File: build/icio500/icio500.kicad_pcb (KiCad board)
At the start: 4 copper layers, 113 x 105 mm, 54 parts, among them J1 ?, U1 ?, U2 ?, U3 ?, U4 ?, U5 ?, U6 ?

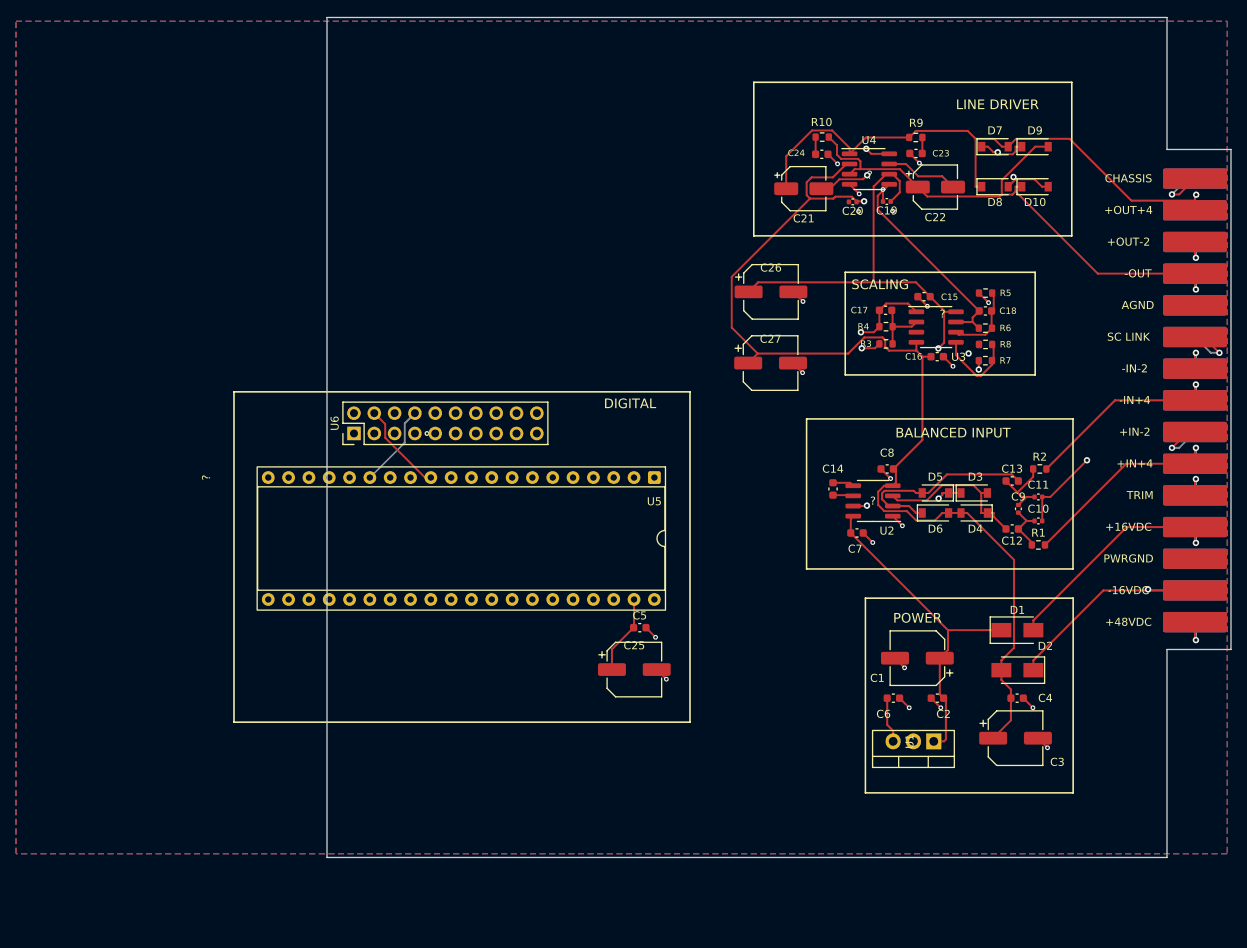
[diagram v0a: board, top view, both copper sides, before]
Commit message: Finalize VPR-500 dimensions and faceplate silkscreen
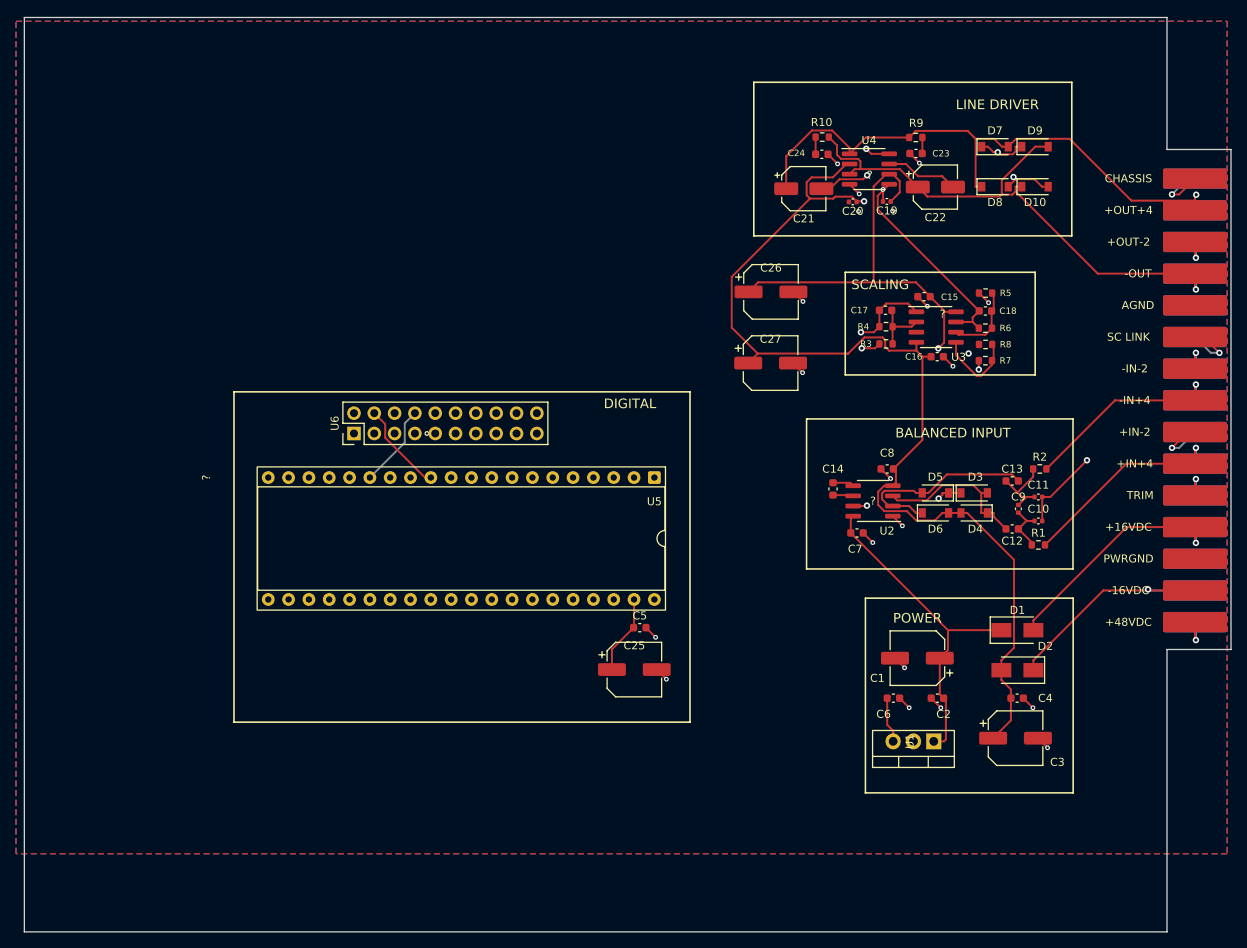
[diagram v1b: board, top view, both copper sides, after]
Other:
- board size 113 x 105 mm -> 150.8 x 114.3 mm
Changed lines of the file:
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@@
 	)
 	(gr_line
-		(start 90 160)
-		(end 90 55)
+		(start 52.17 55)
+		(end 195 55)
 		(stroke
 			(width 0.1)
@@
 	(gr_line
 		(start 195 55)
-		(end 90 55)
-		(stroke
-			(width 0.1)
-			(type default)
-		)
-		(layer "Edge.Cuts")
-	)
-	(gr_line
-		(start 195 71.5)
-		(end 195 55)
+		(end 195 71.5)
 		(stroke
 			(width 0.1)
@@
 		(start 195 71.5)
 		(end 203 71.5)
-		(stroke
-			(width 0.1)
-			(type default)
-		)
-		(layer "Edge.Cuts")
-	)
-	(gr_line
-		(start 195 134)
-		(end 195 160)
-		(stroke
-			(width 0.1)
-			(type default)
-		)
-		(layer "Edge.Cuts")
-	)
-	(gr_line
-		(start 195 160)
-		(end 90 160)
 		(stroke
 			(width 0.1)
@@
 		(stroke
 			(width 0.1)
+			(type default)
+		)
+		(layer "Edge.Cuts")
+	)
+	(gr_line
+		(start 195 134)
+		(end 195 169.3)
+		(stroke
+			(width 0.1)
+			(type default)
+		)
+		(layer "Edge.Cuts")
+	)
+	(gr_line
+		(start 195 169.3)
+		(end 52.17 169.3)
+		(stroke
+			(width 0.1)
+			(type default)
+		)
+		(layer "Edge.Cuts")
+	)
+	(gr_line
+		(start 52.17 169.3)
+		(end 52.17 55)
+		(stroke
+			(width 0.1)

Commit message: Autoroute remaining disconnected pads (GND, faceplate, Daisy)
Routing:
- net gnd: track 32.0 -> 221.5 mm
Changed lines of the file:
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@@
 	)
 	(embedded_fonts no)
+	(segment
+		(start 130.9200 127.7500)
+		(end 129.8700 127.7500)
+		(width 0.4)
+		(layer "F.Cu")
+		(net "gnd")
+	)
+	(segment
+		(start 129.8700 127.7500)
+		(end 129.8700 131.2800)
+		(width 0.4)
+		(layer "F.Cu")
+		(net "gnd")
+	)
+	(segment
+		(start 198.5000 90.9790)
+		(end 172.7000 90.9790)
+		(width 0.4)
+		(layer "F.Cu")
+		(net "gnd")
+	)
+	(segment
+		(start 172.7000 90.9790)
+		(end 172.7000 90.6500)
+		(width 0.4)
+		(layer "F.Cu")
+		(net "gnd")
+	)
+	(segment
+		(start 198.5000 90.9790)
+		(end 172.7000 90.9790)
+		(width 0.4)
+		(layer "F.Cu")
+		(net "gnd")
+	)
+	(segment
+		(start 198.5000 122.6590)
+		(end 178.2400 122.6590)
+		(width 0.4)
+		(layer "F.Cu")
+		(net "gnd")
+	)
+	(segment
+		(start 178.2400 122.6590)
+		(end 178.2400 141.2900)
+		(width 0.4)
+		(layer "F.Cu")
+		(net "gnd")
+	)
+	(segment
+		(start 198.5000 122.6590)
+		(end 178.2400 122.6590)
+		(width 0.4)
+		(layer "F.Cu")
+		(net "gnd")
+	)
+	(segment
+		(start 95.9100 107.0000)
+		(end 129.8700 107.0000)
+		(width 0.4)
+		(layer "F.Cu")
+		(net "gnd")
+	)
+	(segment
+		(start 129.8700 107.0000)
+		(end 129.8700 127.7500)
+		(width 0.4)
+		(layer "F.Cu")
+		(net "gnd")
+	)
+	(segment
+		(start 98.4500 107.0000)
+		(end 95.9100 107.0000)
+		(width 0.4)
+		(layer "F.Cu")
+		(net "gnd")
+	)
+	(segment
+		(start 100.9900 107.0000)
+		(end 98.4500 107.0000)
+		(width 0.4)
+		(layer "F.Cu")
+		(net "gnd")
+	)
+	(segment
+		(start 171.5000 95.8710)
+		(end 170.2000 95.8710)
+		(width 0.4)
+		(layer "F.Cu")
+		(net "gnd")
+	)
+	(segment
+		(start 170.2000 95.8710)
+		(end 170.2000 97.0000)
+		(width 0.4)
+		(layer "F.Cu")
+		(net "gnd")
+	)
+	(segment
+		(start 163.3070 145.4855)
+		(end 162.7800 145.4855)
+		(width 0.4)
+		(layer "F.Cu")
+		(net "gnd")
+	)
+	(segment
+		(start 162.7800 145.4855)
+		(end 162.7800 141.2900)
+		(width 0.4)
+		(layer "F.Cu")
+		(net "gnd")
+	)
+	(segment
+		(start 163.6750 94.3350)
+		(end 165.0500 94.3350)
+		(width 0.4)
+		(layer "F.Cu")
+		(net "gnd")
+	)
+	(segment
+		(start 165.0500 94.3350)
+		(end 165.0500 91.1000)
+		(width 0.4)
+		(layer "F.Cu")
+		(net "gnd")
+	)
+	(segment
+		(start 155.2400 78.0500)
+		(end 156.5300 78.0500)
+		(width 0.4)
+		(layer "F.Cu")
+		(net "gnd")
+	)
+	(segment
+		(start 156.5300 78.0500)
+		(end 156.5300 77.0600)
+		(width 0.4)
+		(layer "F.Cu")
+		(net "gnd")
+	)
 )

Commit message: Revert autorouted traces - board was already fully connected
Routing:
- net gnd: track 221.5 -> 32.0 mm
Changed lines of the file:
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@@
 	)
 	(embedded_fonts no)
-	(segment
-		(start 130.9200 127.7500)
-		(end 129.8700 127.7500)
-		(width 0.4)
-		(layer "F.Cu")
-		(net "gnd")
-	)
-	(segment
-		(start 129.8700 127.7500)
-		(end 129.8700 131.2800)
-		(width 0.4)
-		(layer "F.Cu")
-		(net "gnd")
-	)
-	(segment
-		(start 198.5000 90.9790)
-		(end 172.7000 90.9790)
-		(width 0.4)
-		(layer "F.Cu")
-		(net "gnd")
-	)
-	(segment
-		(start 172.7000 90.9790)
-		(end 172.7000 90.6500)
-		(width 0.4)
-		(layer "F.Cu")
-		(net "gnd")
-	)
-	(segment
-		(start 198.5000 90.9790)
-		(end 172.7000 90.9790)
-		(width 0.4)
-		(layer "F.Cu")
-		(net "gnd")
-	)
-	(segment
-		(start 198.5000 122.6590)
-		(end 178.2400 122.6590)
-		(width 0.4)
-		(layer "F.Cu")
-		(net "gnd")
-	)
-	(segment
-		(start 178.2400 122.6590)
-		(end 178.2400 141.2900)
-		(width 0.4)
-		(layer "F.Cu")
-		(net "gnd")
-	)
-	(segment
-		(start 198.5000 122.6590)
-		(end 178.2400 122.6590)
-		(width 0.4)
-		(layer "F.Cu")
-		(net "gnd")
-	)
-	(segment
-		(start 95.9100 107.0000)
-		(end 129.8700 107.0000)
-		(width 0.4)
-		(layer "F.Cu")
-		(net "gnd")
-	)
-	(segment
-		(start 129.8700 107.0000)
-		(end 129.8700 127.7500)
-		(width 0.4)
-		(layer "F.Cu")
-		(net "gnd")
-	)
-	(segment
-		(start 98.4500 107.0000)
-		(end 95.9100 107.0000)
-		(width 0.4)
-		(layer "F.Cu")
-		(net "gnd")
-	)
-	(segment
-		(start 100.9900 107.0000)
-		(end 98.4500 107.0000)
-		(width 0.4)
-		(layer "F.Cu")
-		(net "gnd")
-	)
-	(segment
-		(start 171.5000 95.8710)
-		(end 170.2000 95.8710)
-		(width 0.4)
-		(layer "F.Cu")
-		(net "gnd")
-	)
-	(segment
-		(start 170.2000 95.8710)
-		(end 170.2000 97.0000)
-		(width 0.4)
-		(layer "F.Cu")
-		(net "gnd")
-	)
-	(segment
-		(start 163.3070 145.4855)
-		(end 162.7800 145.4855)
-		(width 0.4)
-		(layer "F.Cu")
-		(net "gnd")
-	)
-	(segment
-		(start 162.7800 145.4855)
-		(end 162.7800 141.2900)
-		(width 0.4)
-		(layer "F.Cu")
-		(net "gnd")
-	)
-	(segment
-		(start 163.6750 94.3350)
-		(end 165.0500 94.3350)
-		(width 0.4)
-		(layer "F.Cu")
-		(net "gnd")
-	)
-	(segment
-		(start 165.0500 94.3350)
-		(end 165.0500 91.1000)
-		(width 0.4)
-		(layer "F.Cu")
-		(net "gnd")
-	)
-	(segment
-		(start 155.2400 78.0500)
-		(end 156.5300 78.0500)
-		(width 0.4)
-		(layer "F.Cu")
-		(net "gnd")
-	)
-	(segment
-		(start 156.5300 78.0500)
-		(end 156.5300 77.0600)
-		(width 0.4)
-		(layer "F.Cu")
-		(net "gnd")
-	)
 )

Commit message: Fix pre-existing GND/audio_out_to_1646 short: remove orphan stub, relocate via
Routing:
- net gnd: track 32.0 -> 30.5 mm
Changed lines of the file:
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@@
-	)
-	(segment
-		(start 159.5 78)
-		(end 159.5 76.5)
-		(width 0.25)
-		(layer "F.Cu")
-		(net "gnd")
 	)
 	(segment
@@
 	)
 	(via
-		(at 159.5 76.5)
+		(at 157.5 76.5)
 		(size 0.6)
 		(drill 0.3)

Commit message: DRC: fix starved thermals and dangling via (-3 violations)
- Delete dangling via on net 'd14' (UUID df0a3bee) - not connected on any layer
- Add zone_connect solid fill to C19 pad 2 (GND) - fix starved thermal on F.Cu
- Add zone_connect solid fill to U6 pads 5/7/9 (GND) - fix starved thermal on B.Cu
- Set island_removal_mode=1 on F.Cu GND zone - auto-remove isolated fill on refill

Violations: 43 -> 40 (3 fixed: 2x starved_thermal, 1x via_dangling)
Remaining isolated_copper is pre-existing fill geometry issue requiring routing work.
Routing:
- net d14: vias 1 -> 0
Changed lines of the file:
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@@
 			(net "gnd")
 			(pintype "stereo")
-		)
+			(zone_connect 2))
 		(embedded_fonts no)
 		(model "${KISYS3DMOD}/Capacitor_SMD.3dshapes/C_0402_1005Metric.step"
@@
 			(net "gnd")
 			(pintype "stereo")
-		)
+			(zone_connect 2))
 		(pad "4" thru_hole circle
 			(at 2.54 2.54 90)
@@
 			(net "gnd")
 			(pintype "stereo")
-		)
+			(zone_connect 2))
 		(pad "6" thru_hole circle
 			(at 2.54 5.08 90)
@@
 			(net "gnd")
 			(pintype "stereo")
-		)
+			(zone_connect 2))
 		(pad "8" thru_hole circle
 			(at 2.54 7.62 90)
@@
 		(net "d13")
 	)
-	(via
-		(at 102.49 107)
-		(size 0.6)
-		(drill 0.3)
-		(layers "F.Cu" "B.Cu")
-		(net "d14")
-	)
 	(segment
 		(start 101.2066 109.3234)
@@
 			(thermal_gap 0.3)
 			(thermal_bridge_width 0.4)
-			(island_removal_mode 0)
+			(island_removal_mode 1)
 		)
 		(polygon

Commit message: DRC: Route F.Cu GND trace to stitch isolated island
- Replaced the dangling via with a direct F.Cu trace connecting U6 Pad 5 to Pad 7 (both GND).
- This routes directly through the isolated GND island, natively stitching it to the pins without needing any clearances for a new via.
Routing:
- net gnd: track 30.5 -> 33.1 mm
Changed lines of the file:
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@@
+	)
+	(segment
+		(start 98.45 107.0)
+		(end 100.99 107.0)
+		(width 0.25)
+		(layer "F.Cu")
+		(net "gnd")
 	)
 	(segment
@@
 			(thermal_gap 0.3)
 			(thermal_bridge_width 0.4)
-			(island_removal_mode 1)
+			(island_removal_mode 0)
 		)
 		(polygon

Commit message: idk
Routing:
- net gnd: track 33.1 -> 223.5 mm

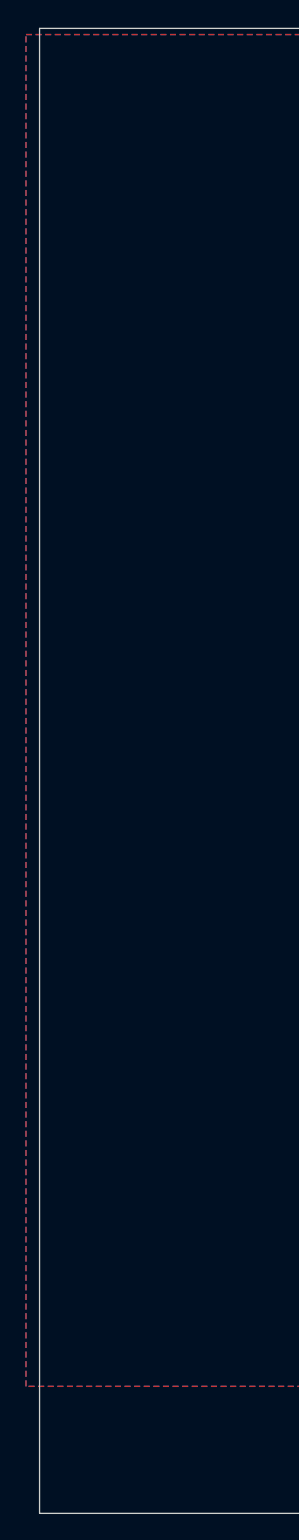
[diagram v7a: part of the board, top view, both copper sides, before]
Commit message: Add VPR-500 mounting holes to front edge of main board
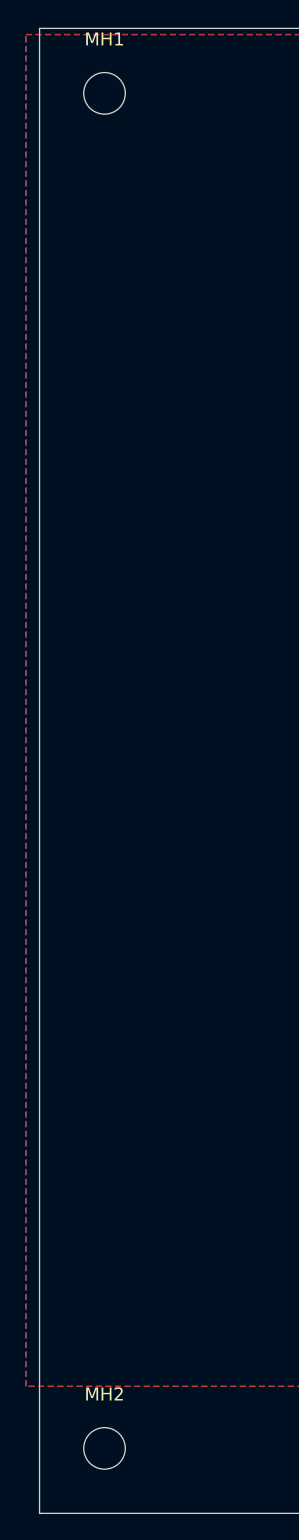
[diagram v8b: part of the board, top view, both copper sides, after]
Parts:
- added MH1: MountingHole_3.2mm_M3, MountingHole_3.2mm_M3, F.Cu at (57.2, 60.0)
- added MH2: MountingHole_3.2mm_M3, MountingHole_3.2mm_M3, F.Cu at (57.2, 164.3)
